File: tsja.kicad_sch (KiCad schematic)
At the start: 66 parts, among them J1 QWIIC, J2 Micro_SD_Card, J3 SAO, J4 EXT, J6 USB-C, M1 Vibration, Q1 AP2302B, Q4 AO3400 (A09T), Q5 AO3400 (A09T), T1 Select, T2 Start, T3 B, T4 A, T5 Cross, U1 74LVC1G17GW,125, U10 SY6280AAC, U11 SK6805, U12 SK6805, U13 SK6805, U14 SK6805, U15 SK6805, U2 MPR121QR2, U3 ESP32-WROVER-E, U7 CH340K, U8 SK6805, U9 SY6280AAC

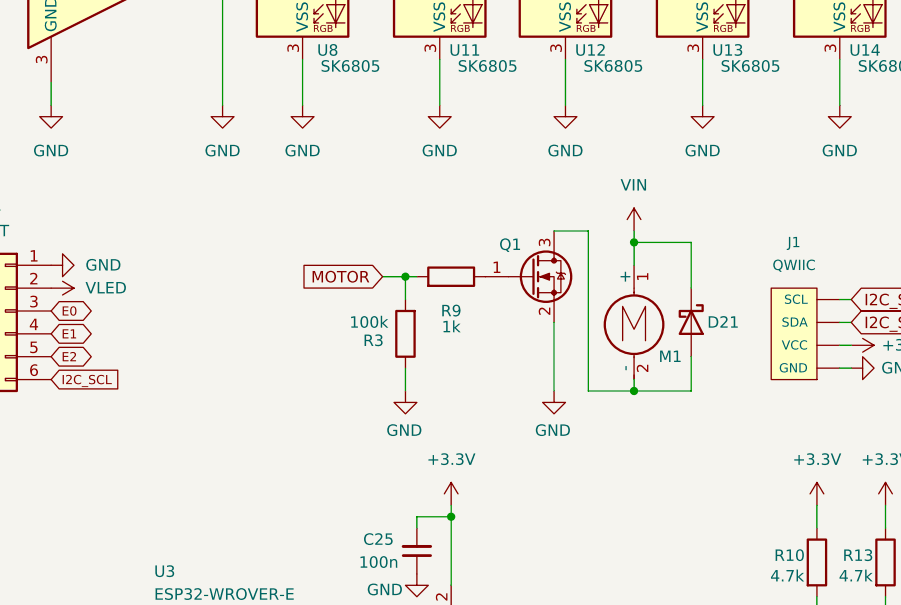
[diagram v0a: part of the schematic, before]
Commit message: Fix some routing issues, add GND vias, add capacitor for M1, add spacing between vias for ground to pour inbetween.
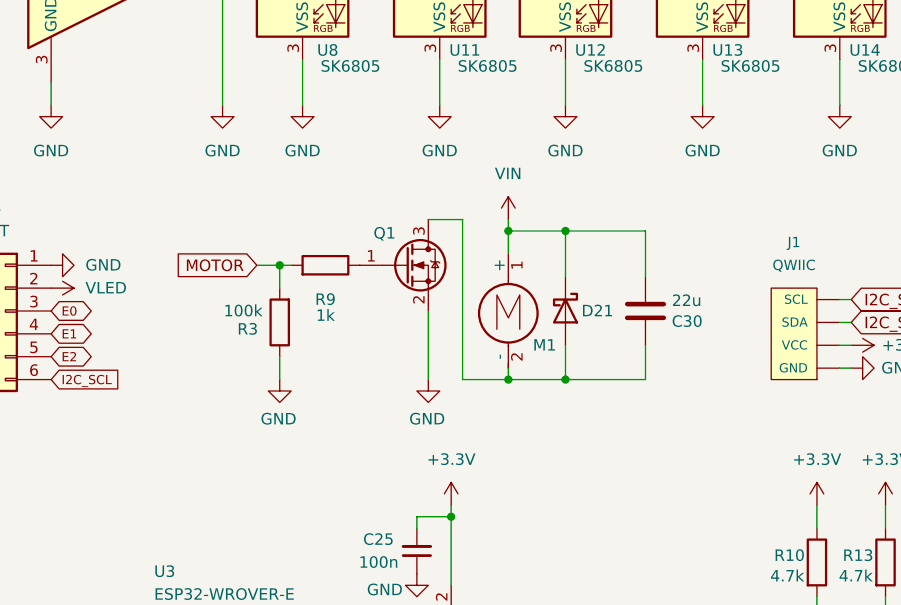
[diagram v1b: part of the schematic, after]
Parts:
- added C30: 22u, Capacitor_SMD:C_0805_2012Metric, symbol mch2021-rescue:C-Device
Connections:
- net VIN: now also C30.2
- net at D21.2 (A), M1.2 (-), Q1.3 (D): now also C30.1
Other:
- moved on the sheet: D21, M1, Q1, R3, R9
